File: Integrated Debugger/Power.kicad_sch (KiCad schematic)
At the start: 23 parts, among them J5 PWR, Q2 Generic N-MOSFET, SW3 Auxiliary Override, SW4 Target Override, U4 TPS7A2633DRVR, U5 TPS22914, U6 TPS22914

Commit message: fix(debugger): relpace picostar 0.4 with 0.65 variant
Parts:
- Q2: footprint PCM_Picoballoon ICs:PICOSTAR-3 -> Picoballoon ICs:PICOSTAR-3_0.65
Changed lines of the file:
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@@
 			)
 		)
-		(property "Footprint" "PCM_Picoballoon ICs:PICOSTAR-3"
+		(property "Footprint" "Picoballoon ICs:PICOSTAR-3_0.65"
 			(at 149.86 31.75 0)
 			(effects

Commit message: Debugger 1.1.2 production files
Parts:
- RN1: footprint Picoballoon Passives:Resistor Pack YC248-JR-07100RL -> Picoballoon Passives:Resistor 0402x8
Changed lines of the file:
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@@
 	(title_block
 		(title "Power supply")
-		(date "2025-11-01")
-		(rev "1.1.1")
+		(date "2025-11-03")
+		(rev "1.1.2")
 	)
 	(rectangle
@@
 			)
 		)
-		(property "Footprint" "Picoballoon Passives:Resistor Pack YC248-JR-07100RL"
+		(property "Footprint" "Picoballoon Passives:Resistor 0402x8"
 			(at 81.28 104.648 90)
 			(effects

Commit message: IDBG schematic
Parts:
- removed C8, C9: 100nF, Picoballoon Passives:Capacitor 0201, symbol Picoballoon Passives:Capacitor
- removed Q2: Generic N-MOSFET, Picoballoon ICs:PICOSTAR-3_0.65, symbol Picoballoon ICs:Generic N-MOSFET
- removed R14, R15: 10kΩ, Picoballoon Passives:Resistor 0201, symbol Picoballoon Passives:Resistor
- removed RN1: 100Ω, Picoballoon Passives:Resistor 0402x8, symbol Picoballoon Passives:Resistor array 8
- removed U4: TPS7A2633DRVR, Picoballoon ICs:WSON-6 2x2mm, symbol Picoballoon ICs:LDO TPS7A26
- removed U5, U6: TPS22914, Picoballoon ICs:DSBGA-4, symbol Picoballoon ICs:TPS22914BYFPR
- added C44, C45: 1µF, Picoballoon Passives:Capacitor 0201, symbol Picoballoon Passives:Capacitor
- added D5, D6: ORANGE, Picoballoon Passives:LED 0201, symbol Picoballoon Passives:LED
- added D7: CFSH05-20L TR PBFREE, Picoballoon Passives:Diode SOD-882, symbol Picoballoon Passives:Schottky Diode
- added R7, R8: 1kΩ, Picoballoon Passives:Resistor 0201, symbol Picoballoon Passives:Resistor
- added U1: TPS7A2633DRVR, Picoballoon ICs:WSON-6 2x2mm, symbol Picoballoon ICs:LDO TLV767
- added U4: MAX40200, Picoballoon ICs:WLP-4, symbol Picoballoon ICs:MAX40200
- added U8, U9: TPS22916, Picoballoon ICs:DSBGA-4, symbol Picoballoon ICs:TPS22916CYFPR
- C10, C16: JLCPCB Part # C76930 -> (none)
- C11, C12, C13, C15: JLCPCB Part # C76934 -> (none)
- C14: value 1μF -> 4.7μF; JLCPCB Part # C76930 -> (none); LCSC Part # C335102 -> C335103; MPN GRM033R61C105ME15D -> GRM035R60J475ME15D
- J5: JLCPCB Part # C177225 -> (none); LCSC Part # C177225 -> C52995100; MPN 532610271 -> WAFA2-RDT1-2021-D
- R16, R17, R18, R19: JLCPCB Part # C717002 -> (none)
- SW3, SW4: JLCPCB Part # C2681570 -> (none)
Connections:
- net AUX_EN: now also U8.B2 (ON)
- net GND: now also C44.2, C45.2, R7.2, R8.2, U1.3 (GND), U1.5 (GND), U1.7 (EXP), U4.B2 (GND), U8.B1 (GND), U9.B1 (GND)
- net TARGET_EN: now also SW4.2
- net +3.3V renamed VDD_3V3
- net VDD_3V3: now also C44.1, C45.1, U1.1 (OUT), U1.2 (SNS), U8.A2 (VIN), U9.A2 (VIN)
- net +5V renamed VDD_USB
- net VDD_USB: now also U1.4 (EN), U1.6 (IN)
- net V_AUX renamed VDD_TG
- net VDD_TG: now also U4.A2 (OUT); no longer C13.1
- net V_TARGET renamed V_TARGET_UNFILT
- net V_TARGET_UNFILT: now also C13.1, D5.1 (K), D6.1 (K), D7.2 (A), U4.A1 (VDD), U4.B1 (EN), U8.A1 (OUT), U9.A1 (OUT)
- new net: D6.2 (A), R8.1
- new net: D5.2 (A), R7.1
- new net TG_EN: U9.B2 (ON)
- new net VDD_AUX: D7.1 (K)
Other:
- note added: "3.3V LDO SYSTEM REGULATOR"
- note removed: "EXTERNAL TARGET POWER SUPPLY"
- note removed: "POWER REGULATION"
- moved on the sheet: C10, C11, C12, C13, C14, C15, C16, J5, R16, R17, R18, R19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

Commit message: Integrated debugger PCB
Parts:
- D5, D6: footprint Picoballoon Passives:LED 0201 -> Picoballoon Passives:LED 0402
- J5: footprint Picoballoon Mechanical & Misc:MOLEX 532610271 -> Picoballoon Mechanical & Misc:JST-SH-2P
- SW3: value Auxiliary Override -> AUXILIARY POWER
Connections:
- net TARGET_EN is gone; now on net TG_EN: SW4.2
- net V_TARGET_UNFILT: no longer names the net of C12.1, D5.1 (K), U4.A1 (VDD), U4.B1 (EN), U9.A1 (OUT)
- net V_TARGET_UNFILT: no longer C13.1, D6.1 (K), D7.2 (A), U8.A1 (OUT)
- new net: C13.1, D6.1 (K), D7.2 (A), U8.A1 (OUT)
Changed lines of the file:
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@@
 		)
 	)
-	(label "V_TARGET_UNFILT"
-		(at 44.45 20.32 0)
-		(effects
-			(font
-				(size 0.254 0.254)
-				(color 255 255 225 1)
-			)
-			(justify left bottom)
-		)
-	)
-	(label "V_TARGET_UNFILT"
-		(at 170.18 20.32 0)
-		(effects
-			(font
-				(size 0.254 0.254)
-				(color 255 255 225 1)
-			)
-			(justify left bottom)
-		)
-	)
 	(hierarchical_label "AUX_EN"
 		(shape input)
@@
 		)
 	)
-	(hierarchical_label "TARGET_EN"
+	(hierarchical_label "TG_EN"
 		(shape input)
 		(at 52.07 74.93 0)
@@
 			)
 		)
-		(property "Footprint" "Picoballoon Passives:LED 0201"
+		(property "Footprint" "Picoballoon Passives:LED 0402"
 			(at 186.69 25.4 0)
 			(effects
@@
 			)
 		)
-		(property "Footprint" "Picoballoon Mechanical & Misc:MOLEX 532610271"
+		(property "Footprint" "Picoballoon Mechanical & Misc:JST-SH-2P"
 			(at 120.65 33.02 0)
 			(effects
@@
 			)
 		)
-		(property "Value" "Auxiliary Override"
+		(property "Value" "AUXILIARY POWER"
 			(at 17.78 67.31 0)
 			(effects
@@
 			)
 		)
-		(property "Footprint" "Picoballoon Passives:LED 0201"
+		(property "Footprint" "Picoballoon Passives:LED 0402"
 			(at 60.96 25.4 0)
 			(effects

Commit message: Reannotate schematic, update GND plane
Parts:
- renumbered C44 to C15, C12 to C16, C10 to C17, C15 to C18, C16 to C19, C11 to C20, C14 to C21, C45 to C22, C13 to C23, R7 to R20, R8 to R21, U9 to U4, U4 to U5, U1 to U6, U8 to U7

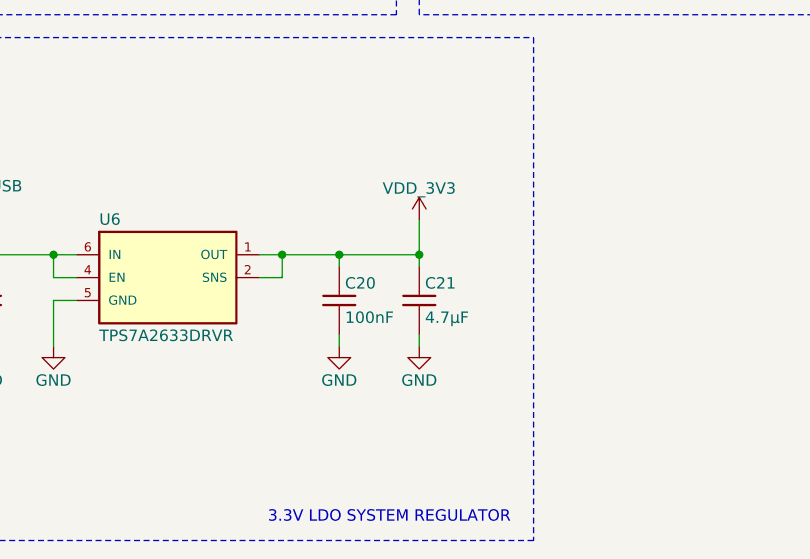
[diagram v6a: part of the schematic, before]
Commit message: led+ resistors updated
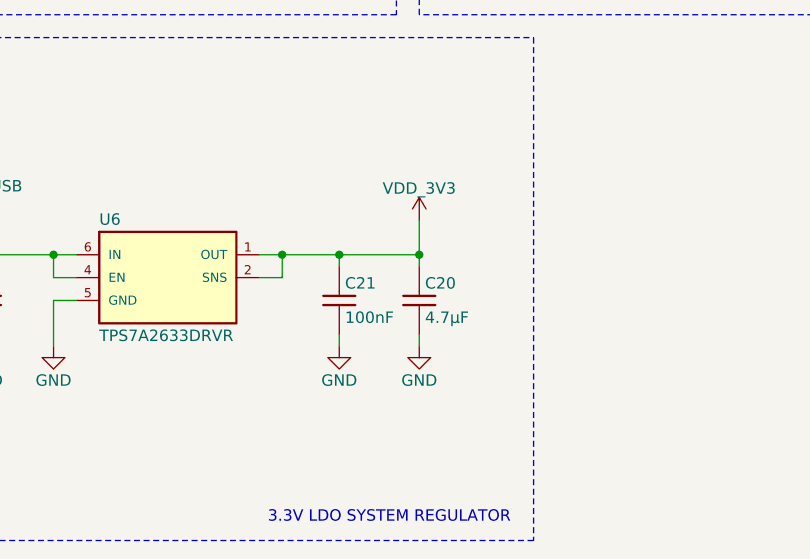
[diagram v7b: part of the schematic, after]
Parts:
- D5, D6: LCSC Part # C5440629 -> C5875753; MPN XL-0201UOC -> APHHS1005SECK
- renumbered C21 to C20, C20 to C21
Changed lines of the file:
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@@
 		(dnp no)
 		(fields_autoplaced yes)
-		(property "Reference" "C21"
+		(property "Reference" "C20"
 			(at 132.715 78.105 0)
 			(do_not_autoplace yes)
@@
 			(project "Integrated Debugger"
 				(path "/ce538ebe-fda9-4af3-9f8c-9fd5bf58f0e4/1f474345-9816-463c-8085-128d97092ac0"
-					(reference "C21")
+					(reference "C20")
 					(unit 1)
 				)
@@
 			)
 		)
-		(property "LCSC Part #" "C5440629"
+		(property "LCSC Part #" "C5875753"
 			(at 186.69 25.4 0)
 			(effects
@@
 			)
 		)
-		(property "MPN" "XL-0201UOC"
+		(property "MPN" "APHHS1005SECK"
 			(at 186.69 25.4 0)
 			(effects
@@
 		(on_board yes)
 		(dnp no)
-		(property "Reference" "C20"
+		(property "Reference" "C21"
 			(at 123.825 78.105 0)
 			(do_not_autoplace yes)
@@
 			(project "Integrated Debugger"
 				(path "/ce538ebe-fda9-4af3-9f8c-9fd5bf58f0e4/1f474345-9816-463c-8085-128d97092ac0"
-					(reference "C20")
+					(reference "C21")
 					(unit 1)
 				)
@@
 			)
 		)
-		(property "LCSC Part #" "C5440629"
+		(property "LCSC Part #" "C5875753"
 			(at 60.96 25.4 0)
 			(effects
@@
 			)
 		)
-		(property "MPN" "XL-0201UOC"
+		(property "MPN" "APHHS1005SECK"
 			(at 60.96 25.4 0)
 			(effects

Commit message: Fix 3D models, add approvals
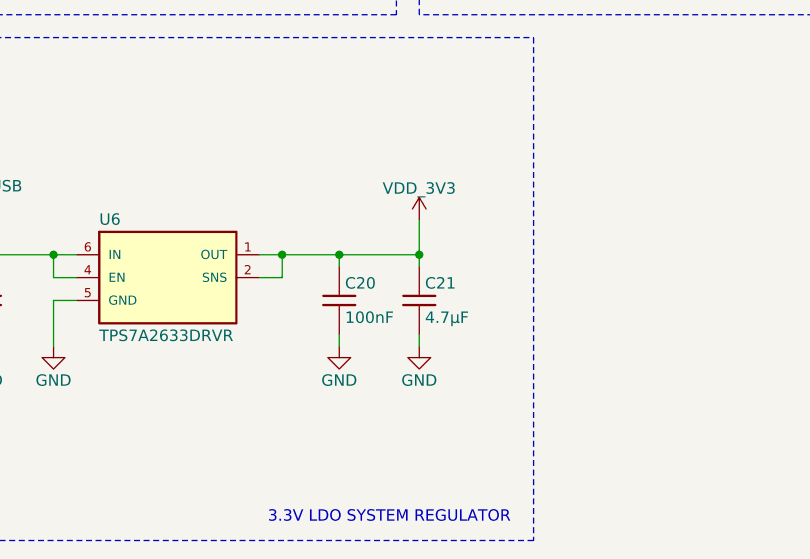
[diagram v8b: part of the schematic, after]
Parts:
- renumbered C21 to C20, C20 to C21
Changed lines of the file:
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@@
 	(title_block
 		(title "Power supply")
-		(date "2026-03-26")
+		(date "2026-03-30")
 		(rev "2.0.0")
 	)
@@
 		(dnp no)
 		(fields_autoplaced yes)
-		(property "Reference" "C20"
+		(property "Reference" "C21"
 			(at 132.715 78.105 0)
 			(do_not_autoplace yes)
@@
 			(project "Integrated Debugger"
 				(path "/ce538ebe-fda9-4af3-9f8c-9fd5bf58f0e4/1f474345-9816-463c-8085-128d97092ac0"
-					(reference "C20")
+					(reference "C21")
 					(unit 1)
 				)
@@
 		(on_board yes)
 		(dnp no)
-		(property "Reference" "C21"
+		(property "Reference" "C20"
 			(at 123.825 78.105 0)
 			(do_not_autoplace yes)
@@
 			(project "Integrated Debugger"
 				(path "/ce538ebe-fda9-4af3-9f8c-9fd5bf58f0e4/1f474345-9816-463c-8085-128d97092ac0"
-					(reference "C21")
+					(reference "C20")
 					(unit 1)
 				)
